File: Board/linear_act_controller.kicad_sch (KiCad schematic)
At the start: 29 parts, among them J1 SSV, J2 ACTUATOR, J3 PROG, J4 PWR_LED, J5 STATUS_LED, J6 PWR_LED, J7 PWR_LED, Q9 IRLML6344TRPBF

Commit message: Silkscreen done.
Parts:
- added U5: ~, Logos:taz, symbol Logos:Logo_TAZ
- renumbered C1 to C22, C2 to C23, D2 to D4, H4 to H2, H2 to H3, H3 to H4, J4 to J2, J5 to J3, J2 to J4, J3 to J5, Q9 to Q1, R36 to R1, R3 to R15, R4 to R17, R16 to R2, R5 to R22, R8 to R23, R7 to R24, R6 to R25, R24 to R3, R1 to R4, R2 to R5
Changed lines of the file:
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@@
 		(on_board yes)
 		(dnp no)
-		(property "Reference" "J2"
+		(property "Reference" "J4"
 			(at 33.782 79.6177 0)
 			(effects
@@
 			(project "linear_act_controller"
 				(path "/a7f12679-28d2-4dcb-a620-9ebf42b92b51"
-					(reference "J2")
+					(reference "J4")
 					(unit 1)
 				)
@@
 		(on_board yes)
 		(dnp no)
-		(property "Reference" "R1"
+		(property "Reference" "R4"
 			(at 58.6486 36.9316 0)
 			(effects
@@
 			(project "linear_act_controller"
 				(path "/a7f12679-28d2-4dcb-a620-9ebf42b92b51"
-					(reference "R1")
+					(reference "R4")
 					(unit 1)
 				)
@@
 		(on_board yes)
 		(dnp no)
-		(property "Reference" "J5"
+		(property "Reference" "J3"
 			(at 147.32 80.264 0)
 			(effects
@@
 			(project "linear_act_controller"
 				(path "/a7f12679-28d2-4dcb-a620-9ebf42b92b51"
-					(reference "J5")
+					(reference "J3")
 					(unit 1)
 				)
@@
 		(on_board yes)
 		(dnp no)
-		(property "Reference" "Q9"
+		(property "Reference" "Q1"
 			(at 153.543 90.2278 0)
 			(effects
@@
 			(project "linear_act_controller"
 				(path "/a7f12679-28d2-4dcb-a620-9ebf42b92b51"
-					(reference "Q9")
+					(reference "Q1")
 					(unit 1)
 				)
@@
 		(on_board yes)
 		(dnp no)
-		(property "Reference" "R4"
+		(property "Reference" "R17"
 			(at 58.6486 95.3516 0)
 			(effects
@@
 			(project "linear_act_controller"
 				(path "/a7f12679-28d2-4dcb-a620-9ebf42b92b51"
-					(reference "R4")
+					(reference "R17")
 					(unit 1)
 				)
@@
 		(on_board yes)
 		(dnp no)
-		(property "Reference" "C1"
+		(property "Reference" "C22"
 			(at 67.1068 44.5516 0)
 			(effects
@@
 			(project "linear_act_controller"
 				(path "/a7f12679-28d2-4dcb-a620-9ebf42b92b51"
-					(reference "C1")
+					(reference "C22")
 					(unit 1)
 				)
@@
 		(on_board yes)
 		(dnp no)
-		(property "Reference" "R5"
+		(property "Reference" "R22"
 			(at 58.674 134.874 90)
 			(effects
@@
 			(project "linear_act_controller"
 				(path "/a7f12679-28d2-4dcb-a620-9ebf42b92b51"
-					(reference "R5")
+					(reference "R22")
 					(unit 1)
 				)
@@
 		(on_board yes)
 		(dnp yes)
-		(property "Reference" "J3"
+		(property "Reference" "J5"
 			(at 40.132 138.43 0)
 			(effects
@@
 			(project "linear_act_controller"
 				(path "/a7f12679-28d2-4dcb-a620-9ebf42b92b51"
-					(reference "J3")
+					(reference "J5")
 					(unit 1)
 				)
@@
 		(on_board yes)
 		(dnp no)
-		(property "Reference" "R3"
+		(property "Reference" "R15"
 			(at 58.6486 87.7316 0)
 			(effects
@@
 			(project "linear_act_controller"
 				(path "/a7f12679-28d2-4dcb-a620-9ebf42b92b51"
-					(reference "R3")
+					(reference "R15")
 					(unit 1)
 				)
@@
 		(dnp no)
 		(fields_autoplaced yes)
-		(property "Reference" "R36"
+		(property "Reference" "R1"
 			(at 165.862 96.5778 0)
 			(effects
@@
 			(project "linear_act_controller"
 				(path "/a7f12679-28d2-4dcb-a620-9ebf42b92b51"
-					(reference "R36")
+					(reference "R1")
 					(unit 1)
 				)
@@
 		(on_board yes)
 		(dnp no)
-		(property "Reference" "R7"
+		(property "Reference" "R24"
 			(at 53.34 142.748 90)
 			(effects
@@
 			(project "linear_act_controller"
 				(path "/a7f12679-28d2-4dcb-a620-9ebf42b92b51"
-					(reference "R7")
+					(reference "R24")
 					(unit 1)
 				)
@@
 		(on_board yes)
 		(dnp no)
-		(property "Reference" "H2"
+		(property "Reference" "H3"
 			(at 37.846 168.148 90)
 			(effects
@@
 			(project "linear_act_controller"
 				(path "/a7f12679-28d2-4dcb-a620-9ebf42b92b51"
-					(reference "H2")
+					(reference "H3")
 					(unit 1)
 				)
@@
 		(dnp no)
 		(fields_autoplaced yes)
-		(property "Reference" "D2"
+		(property "Reference" "D4"
 			(at 82.55 95.2499 90)
 			(effects
@@
 			(project "linear_act_controller"
 				(path "/a7f12679-28d2-4dcb-a620-9ebf42b92b51"
-					(reference "D2")
+					(reference "D4")
 					(unit 1)
 				)
@@
 		(on_board yes)
 		(dnp no)
-		(property "Reference" "C2"
+		(property "Reference" "C23"
 			(at 67.1068 95.3516 0)
 			(effects
@@
 			(project "linear_act_controller"
 				(path "/a7f12679-28d2-4dcb-a620-9ebf42b92b51"
-					(reference "C2")
+					(reference "C23")
 					(unit 1)
 				)
@@
 		(on_board yes)
 		(dnp no)
-		(property "Reference" "H3"
+		(property "Reference" "H4"
 			(at 37.846 178.308 90)
 			(effects
@@
 			(project "linear_act_controller"
 				(path "/a7f12679-28d2-4dcb-a620-9ebf42b92b51"
-					(reference "H3")
+					(reference "H4")
 					(unit 1)
 				)
@@
 		(on_board yes)
 		(dnp no)
-		(property "Reference" "R24"
+		(property "Reference" "R3"
 			(at 157.7086 77.5716 0)
 			(effects
@@
 			(project "linear_act_controller"
 				(path "/a7f12679-28d2-4dcb-a620-9ebf42b92b51"
-					(reference "R24")
+					(reference "R3")
 					(unit 1)
 				)
@@
 		(on_board yes)
 		(dnp no)
-		(property "Reference" "R8"
+		(property "Reference" "R23"
 			(at 58.42 149.352 90)
 			(effects
@@
 			(project "linear_act_controller"
 				(path "/a7f12679-28d2-4dcb-a620-9ebf42b92b51"
-					(reference "R8")
+					(reference "R23")
+					(unit 1)
+				)
+			)
+		)
+	)
+	(symbol
+		(lib_id "Logos:Logo_TAZ")
+		(at 63.5 177.8 0)
+		(unit 1)
+		(exclude_from_sim no)
+		(in_bom no)
+		(on_board yes)
+		(dnp no)
+		(fields_autoplaced yes)
+		(property "Reference" "U5"
+			(at 65.879 174.7908 0)
+			(effects
+				(font
+					(size 1.27 1.27)
+				)
+				(justify left)
+			)
+		)
+		(property "Value" "~"
+			(at 65.879 176.4722 0)
+			(effects
+				(font
+					(size 1.27 1.27)
+				)
+				(justify left)
+			)
+		)
+		(property "Footprint" "Logos:taz"
+			(at 63.5 177.8 0)
+			(effects
+				(font
+					(size 1.27 1.27)
+				)
+				(hide yes)
+			)
+		)
+		(property "Datasheet" ""
+			(at 63.5 177.8 0)
+			(effects
+				(font
+					(size 1.27 1.27)
+				)
+				(hide yes)
+			)
+		)
+		(property "Description" ""
+			(at 63.5 177.8 0)
+			(effects
+				(font
+					(size 1.27 1.27)
+				)
+				(hide yes)
+			)
+		)
+		(instances
+			(project ""
+				(path "/a7f12679-28d2-4dcb-a620-9ebf42b92b51"
+					(reference "U5")
 					(unit 1)
 				)
@@
 		(on_board yes)
 		(dnp no)
-		(property "Reference" "J4"
+		(property "Reference" "J2"
 			(at 153.416 34.29 0)
 			(effects
@@
 			(project ""
 				(path "/a7f12679-28d2-4dcb-a620-9ebf42b92b51"
-					(reference "J4")
+					(reference "J2")
 					(unit 1)
 				)
@@
 		(on_board yes)
 		(dnp no)
-		(property "Reference" "R16"
+		(property "Reference" "R2"
 			(at 164.0586 31.8516 0)
 			(effects
@@
 			(project "linear_act_controller"
 				(path "/a7f12679-28d2-4dcb-a620-9ebf42b92b51"
-					(reference "R16")
+					(reference "R2")
 					(unit 1)
 				)
@@
 		(on_board yes)
 		(dnp no)
-		(property "Reference" "R2"
+		(property "Reference" "R5"
 			(at 58.6486 44.5516 0)
 			(effects
@@
 			(project "linear_act_controller"
 				(path "/a7f12679-28d2-4dcb-a620-9ebf42b92b51"
-					(reference "R2")
+					(reference "R5")
 					(unit 1)
 				)
@@
 		(on_board yes)
 		(dnp no)
-		(property "Reference" "R6"
+		(property "Reference" "R25"
 			(at 58.42 140.208 90)
 			(effects
@@
 			(project "linear_act_controller"
 				(path "/a7f12679-28d2-4dcb-a620-9ebf42b92b51"
-					(reference "R6")
+					(reference "R25")
 					(unit 1)
 				)
@@
 		(on_board yes)
 		(dnp no)
-		(property "Reference" "H4"
+		(property "Reference" "H2"
 			(at 37.846 183.388 90)
 			(effects
@@
 			(project "linear_act_controller"
 				(path "/a7f12679-28d2-4dcb-a620-9ebf42b92b51"
-					(reference "H4")
-					(unit 1)
-				)
+					(reference "H2")
+					(unit 1)
+				)

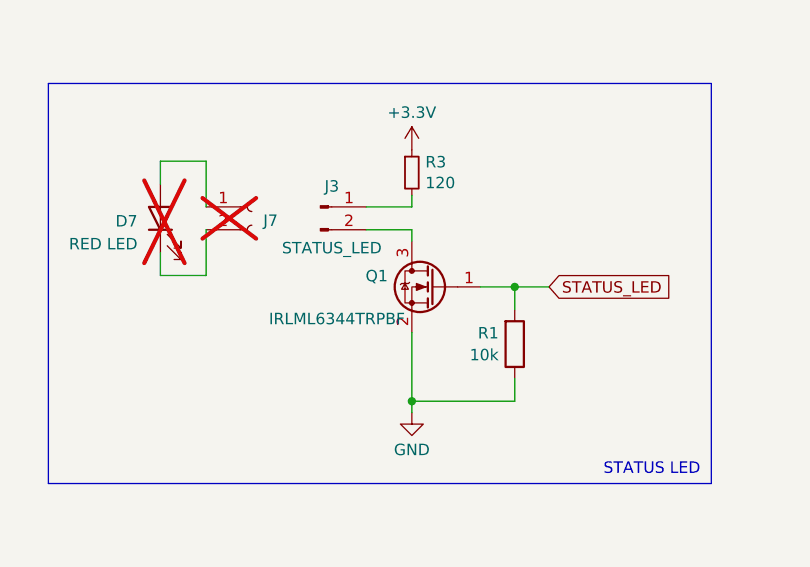
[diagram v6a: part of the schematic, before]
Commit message: Changed some components based on availability.
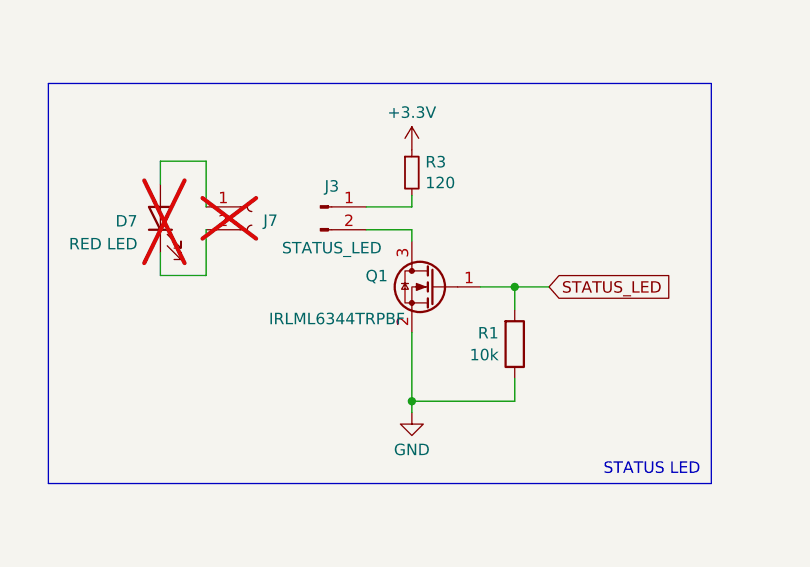
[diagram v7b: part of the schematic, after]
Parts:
- Q1: footprint Package_TO_SOT_SMD:SOT-23_Handsoldering -> Package_TO_SOT_SMD:SOT-23

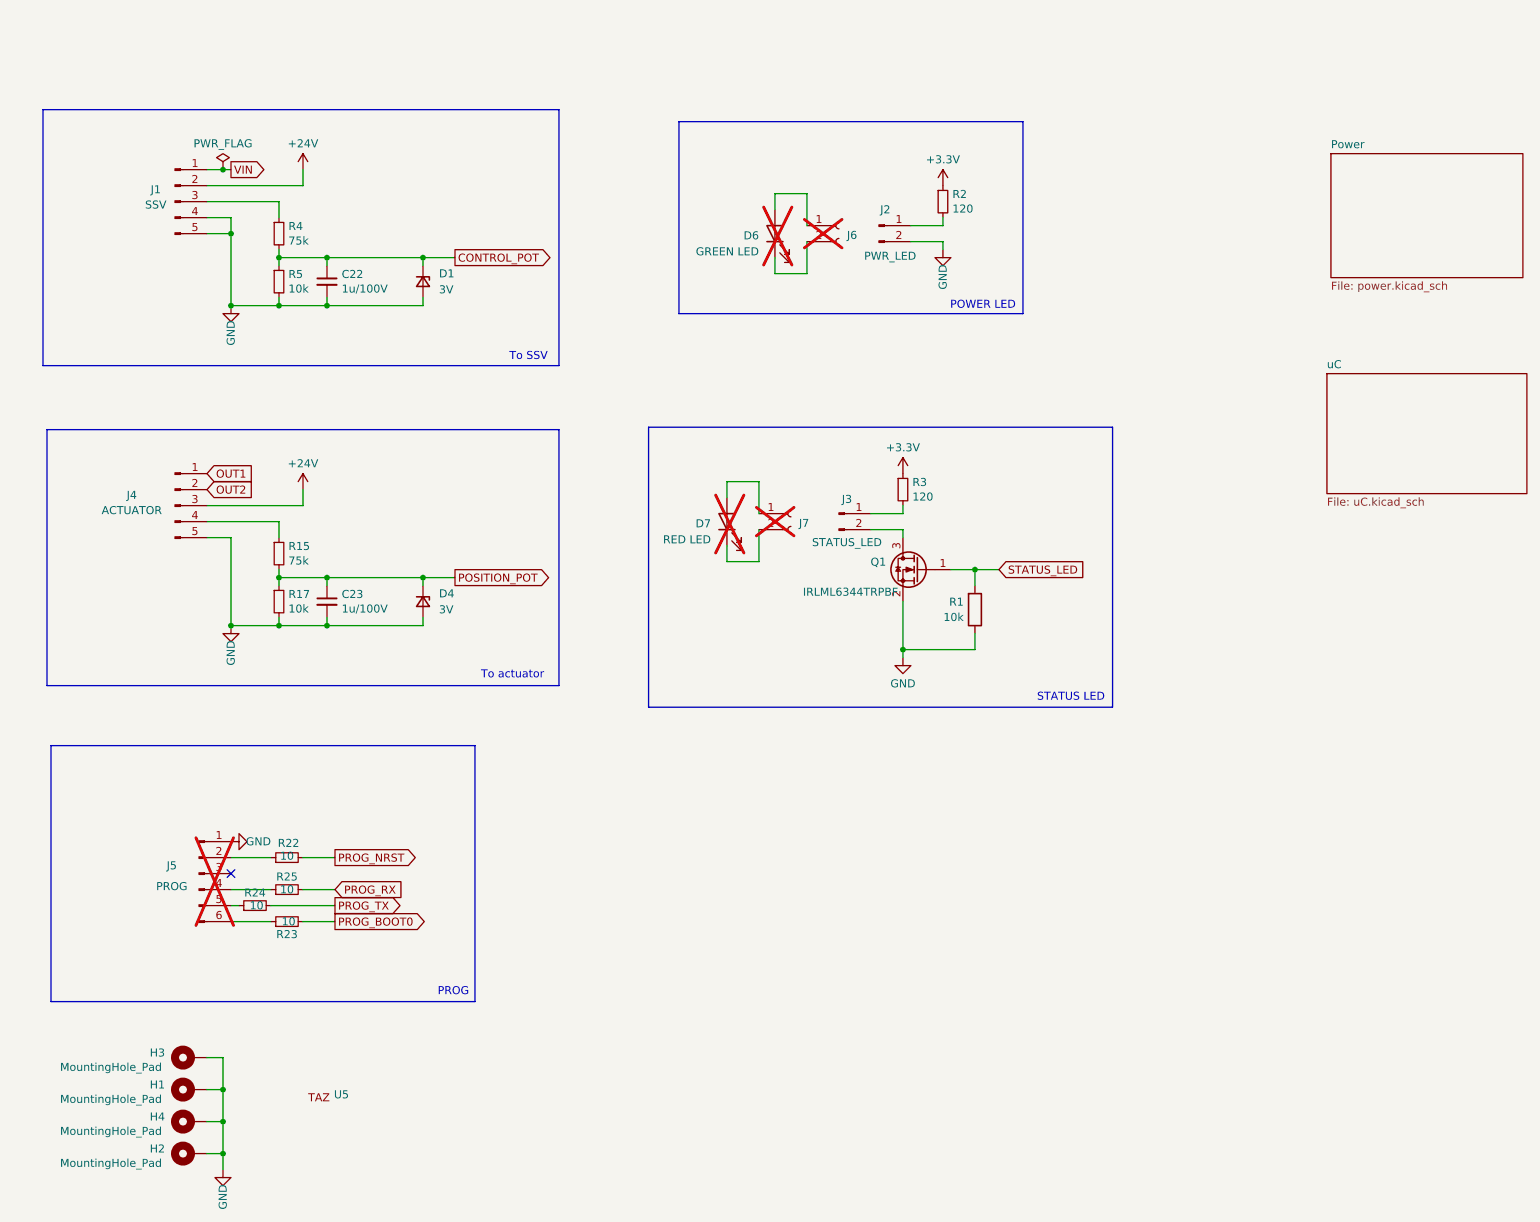
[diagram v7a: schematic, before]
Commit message: Split "SSV" connector into "PWR" and "CONTROL"
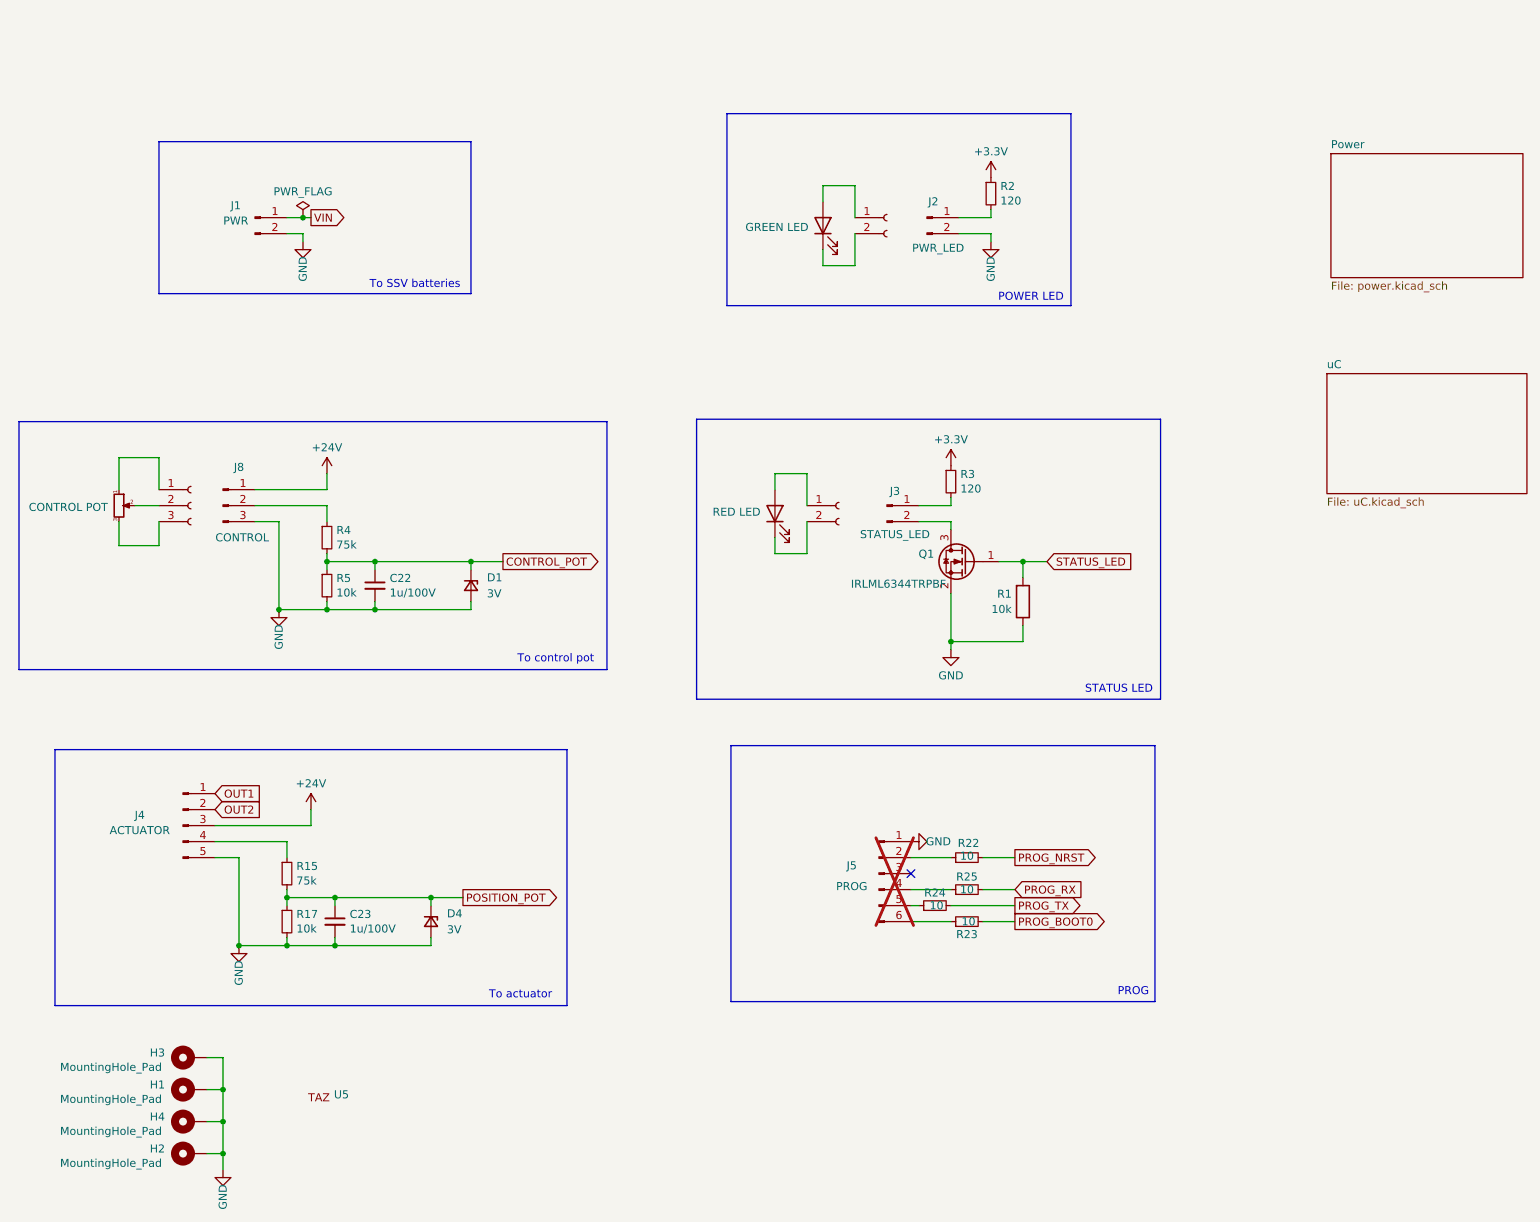
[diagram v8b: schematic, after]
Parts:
- added J8: CONTROL, Connector_JST:JST_XH_B3B-XH-A_1x03_P2.50mm_Vertical, symbol Connector:Conn_01x03_Pin
- added J9: Conn_01x03_Socket, symbol Connector:Conn_01x03_Socket
- added RV1: CONTROL POT, symbol Device:R_Potentiometer_Small
- D6, D7, J6, J7: now fitted; now left out of the parts list
- J1: value SSV -> PWR; footprint Connector_JST:JST_XH_B5B-XH-A_1x05_P2.50mm_Vertical -> Connector_JST:JST_XH_B2B-XH-A_1x02_P2.50mm_Vertical; symbol Connector:Conn_01x05_Pin -> Connector:Conn_01x02_Pin
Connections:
- net +24V: now also J8.1 (Pin_1); no longer J1.2 (Pin_2)
- net GND: now also J1.2 (Pin_2), J8.3 (Pin_3); no longer J1.4 (Pin_4), J1.5 (Pin_5)
- net at R4.1: now also J8.2 (Pin_2); no longer J1.3 (Pin_3)
- new net: J9.1 (Pin_1), RV1.1
- new net: J9.2 (Pin_2), RV1.2
- new net: J9.3 (Pin_3), RV1.3
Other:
- note added: "To SSV batteries"
- note added: "To control pot"
- note removed: "To SSV"
- moved on the sheet: C22, C23, D1, D4, J2, J3, J4, J5, Q1, R1, R15, R17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
